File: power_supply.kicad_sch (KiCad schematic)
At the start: 0 parts

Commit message: Added symbol and footprint for CW308 connector
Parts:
- added U2: LD1117S12TR_SOT223, Package_TO_SOT_SMD:SOT-223-3_TabPin2, symbol Regulator_Linear:LD1117S12TR_SOT223
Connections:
- new net +5V: U2.3 (VI)
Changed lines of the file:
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@@
 	(generator_version "9.0")
 	(paper "A4")
+	(wire
+		(pts
+			(xy 48.26 35.56) (xy 48.26 40.64)
+		)
+		(stroke
+			(width 0)
+			(type default)
+		)
+	)
+	(wire
+		(pts
+			(xy 48.26 40.64) (xy 66.04 40.64)
+		)
+		(stroke
+			(width 0)
+			(type default)
+		)
+	)
+	(symbol
+		(lib_id "Regulator_Linear:LD1117S12TR_SOT223")
+		(at 73.66 40.64 0)
+		(unit 1)
+		(exclude_from_sim no)
+		(in_bom yes)
+		(on_board yes)
+		(dnp no)
+		(fields_autoplaced yes)
+		(property "Reference" "U2"
+			(at 73.66 34.29 0)
+			(effects
+				(font
+					(size 1.27 1.27)
+				)
+			)
+		)
+		(property "Value" "LD1117S12TR_SOT223"
+			(at 73.66 36.83 0)
+			(effects
+				(font
+					(size 1.27 1.27)
+				)
+			)
+		)
+		(property "Footprint" "Package_TO_SOT_SMD:SOT-223-3_TabPin2"
+			(at 73.66 35.56 0)
+			(effects
+				(font
+					(size 1.27 1.27)
+				)
+				(hide yes)
+			)
+		)
+		(property "Datasheet" "http://www.st.com/st-web-ui/static/active/en/resource/technical/document/datasheet/CD00000544.pdf"
+			(at 76.2 46.99 0)
+			(effects
+				(font
+					(size 1.27 1.27)
+				)
+				(hide yes)
+			)
+		)
+		(property "Description" "800mA Fixed Low Drop Positive Voltage Regulator, Fixed Output 1.2V, SOT-223"
+			(at 73.66 40.64 0)
+			(effects
+				(font
+					(size 1.27 1.27)
+				)
+				(hide yes)
+			)
+		)
+		(pin "1"
+		)
+		(pin "3"
+		)
+		(pin "2"
+		)
+		(instances
+			(project ""
+				(path "/e33bf8ee-d1a9-4f5f-9315-873bed2c8796/2ae7c551-db62-4df5-bb63-a75800c2b890"
+					(reference "U2")
+					(unit 1)
+				)
+			)
+		)
+	)
+	(symbol
+		(lib_id "power:+5V")
+		(at 48.26 35.56 0)
+		(unit 1)
+		(exclude_from_sim no)
+		(in_bom yes)
+		(on_board yes)
+		(dnp no)
+		(fields_autoplaced yes)
+		(property "Reference" "#PWR05"
+			(at 48.26 39.37 0)
+			(effects
+				(font
+					(size 1.27 1.27)
+				)
+				(hide yes)
+			)
+		)
+		(property "Value" "+5V"
+			(at 48.26 30.48 0)
+			(effects
+				(font
+					(size 1.27 1.27)
+				)
+			)
+		)
+		(property "Footprint" ""
+			(at 48.26 35.56 0)
+			(effects
+				(font
+					(size 1.27 1.27)
+				)
+				(hide yes)
+			)
+		)
+		(property "Datasheet" ""
+			(at 48.26 35.56 0)
+			(effects
+				(font
+					(size 1.27 1.27)
+				)
+				(hide yes)
+			)
+		)
+		(property "Description" "Power symbol creates a global label with name \"+5V\""
+			(at 48.26 35.56 0)
+			(effects
+				(font
+					(size 1.27 1.27)
+				)
+				(hide yes)
+			)
+		)
+		(pin "1"
+		)
+		(instances
+			(project ""
+				(path "/e33bf8ee-d1a9-4f5f-9315-873bed2c8796/2ae7c551-db62-4df5-bb63-a75800c2b890"
+					(reference "#PWR05")
+					(unit 1)
+				)
+			)
+		)
+	)
 )

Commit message: Development of power source
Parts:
- added C1, C10, C13, C16, C19, C3, C5, C7: 0.1uF, symbol Device:C
- added C11, C14, C17, C2, C20, C4, C6, C8: 10nF, symbol Device:C
- added C12, C15, C18, C21, C9: 4.7uF, symbol Device:C
- added C24, C25, C26, C27, C29: 2.2uF, symbol Device:C
- added C28: 100nF, symbol Device:C
- added R1, R2, R3, R4: 0R, symbol Device:R
- added R10: 470R, symbol Device:R
- added R9: 22R, symbol Device:R
- added TP1, TP2, TP3, TP4, TP5: TestPoint, symbol Connector:TestPoint
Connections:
- net +5V: now also C24.1, C25.1
- net at U2.1 (GND): now also C29.1, R10.1, R9.1
- net VCC_INT_CORE: now reaches U2.2 (VO)
- net VCC_INT_CORE: now also C26.1, C27.1, C28.1, R10.2
- new net GND: C1.2, C10.2, C11.2, C12.2, C13.2, C14.2, C15.2, C16.2, C17.2, C18.2, C19.2, C2.2, C20.2, C21.2, C24.2, C25.2, C26.2, C27.2, C28.2, C29.2, C3.2, C4.2, C5.2, C6.2, C7.2, C8.2, C9.2, R9.2
- new net VDD_HV: R1.1, R2.1, R3.1, R4.1, TP5.1
- new net VDD_HV_FLASH: C3.1, C4.1, R2.2, TP2.1
- new net VDD_HV_IO_FLEX: C5.1, C6.1, R3.2, TP3.1
- new net VDD_HV_JTAG_OSC: C1.1, C2.1, R1.2, TP1.1
- new net VDD_IO_MAIN: C10.1, C11.1, C12.1, C13.1, C14.1, C15.1, C16.1, C17.1, C18.1, C19.1, C20.1, C21.1, C7.1, C8.1, C9.1, R4.2, TP4.1

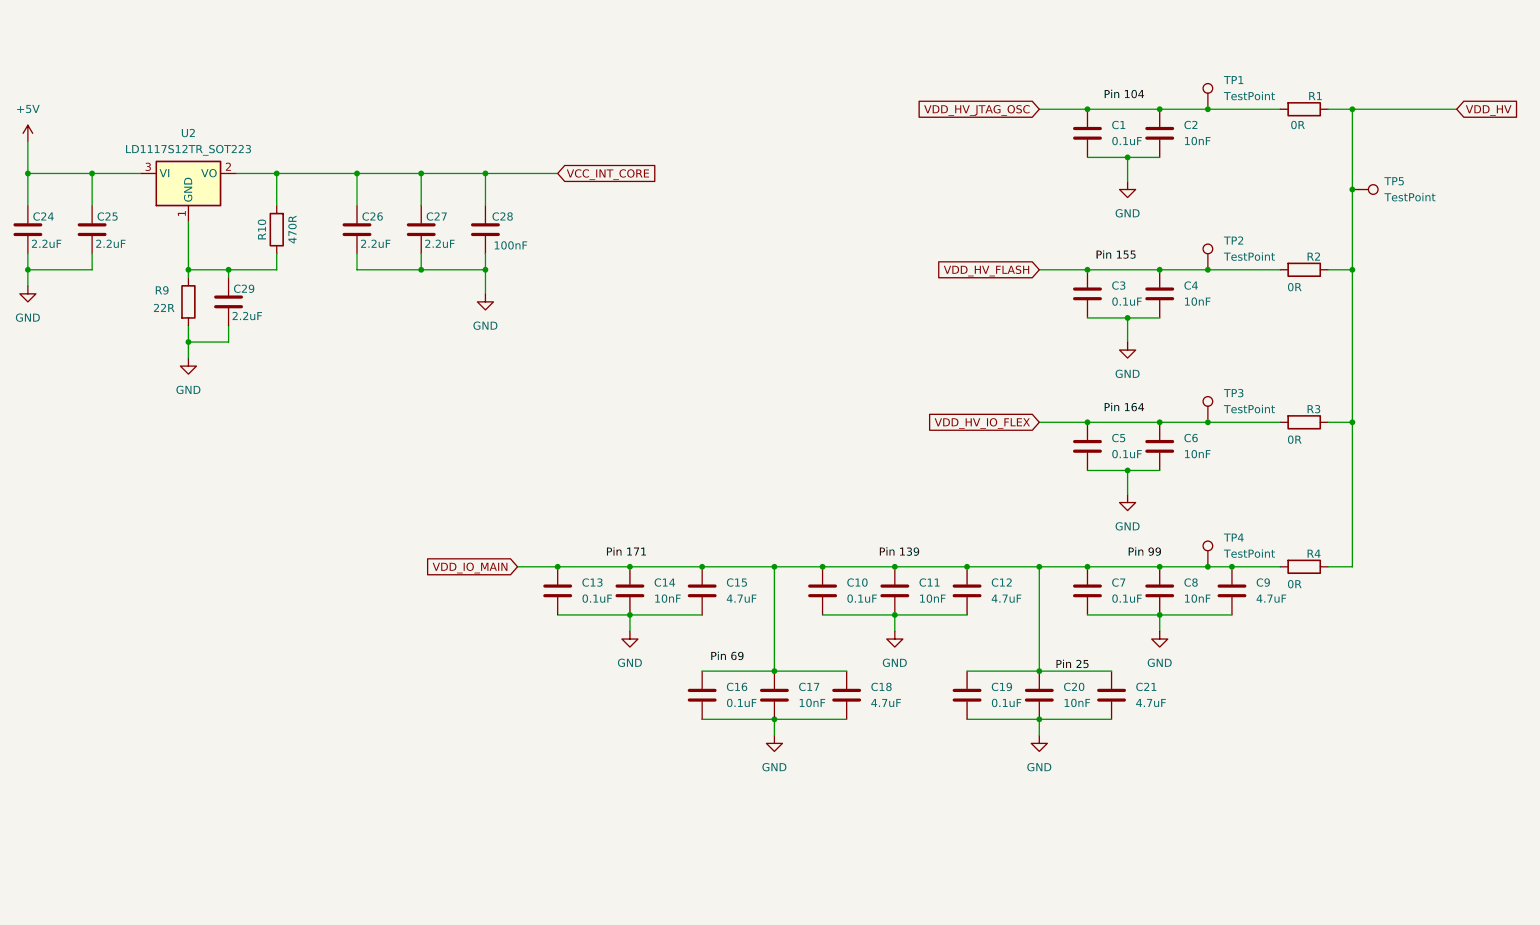
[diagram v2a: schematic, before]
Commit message: Added CAN Bus schematic
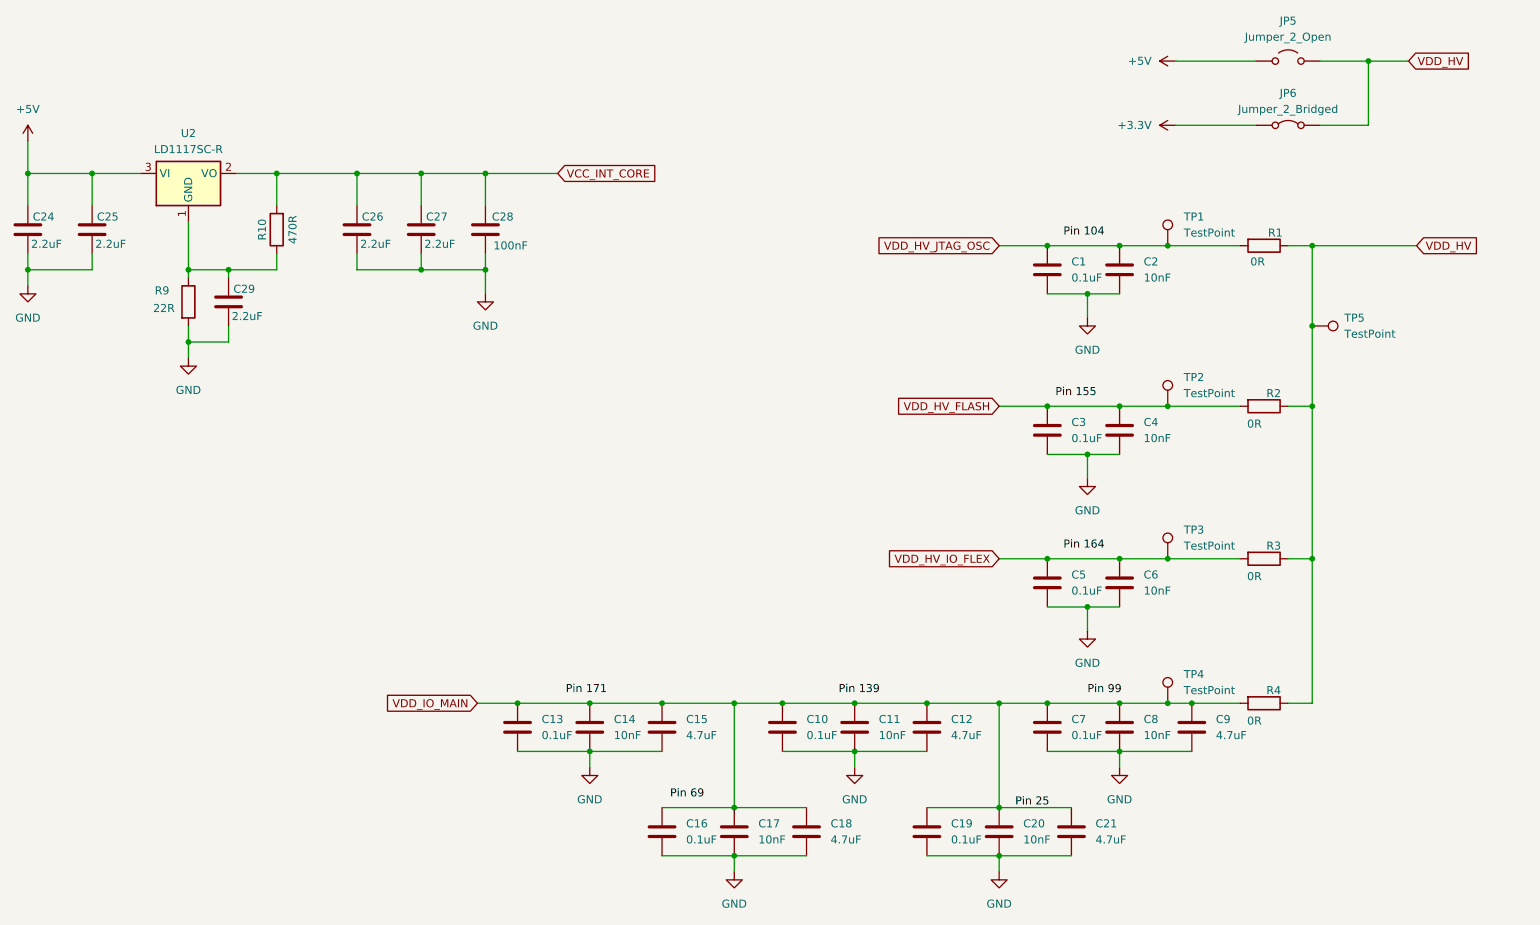
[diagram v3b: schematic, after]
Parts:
- added JP5: Jumper_2_Open, symbol Jumper:Jumper_2_Open
- added JP6: Jumper_2_Bridged, symbol Jumper:Jumper_2_Bridged
- U2: value LD1117S12TR_SOT223 -> LD1117SC-R
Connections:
- net +5V: now also JP5.1 (A)
- net VDD_HV: now also JP5.2 (B), JP6.2 (B)
- new net +3.3V: JP6.1 (A)
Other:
- moved on the sheet: C1, C10, C11, C12, C13, C14, C15, C16, C17, C18, C19, C2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

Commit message: Development backup
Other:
- note added: "1V3"
- note added: "Resistive divider to generate 1.3V output"
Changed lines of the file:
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@@
 	(generator_version "10.0")
 	(paper "A4")
+	(text "1V3"
+		(exclude_from_sim no)
+		(at 128.27 39.37 0)
+		(effects
+			(font
+				(size 1.27 1.27)
+			)
+		)
+	)
+	(text "Resistive divider to generate 1.3V output"
+		(exclude_from_sim no)
+		(at 73.406 30.48 0)
+		(effects
+			(font
+				(size 1.27 1.27)
+			)
+		)
+	)
 	(junction
 		(at 215.9 85.09)
